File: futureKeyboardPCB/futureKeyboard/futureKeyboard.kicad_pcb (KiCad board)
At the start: 2 copper layers, 106 parts, among them J1 Conn_01x01, J10 Conn_01x02, J11 Conn_01x01, J12 Conn_01x01, J13 Conn_01x04, J14 Conn_01x06, J15 Conn_01x06, J16 Conn_01x01, J2 Conn_01x04, J3 Conn_01x01, J4 Conn_01x01, J5 Conn_01x04, J6 Conn_01x06, J7 Conn_01x06, J8 Conn_01x01, J9 Conn_01x01, P1 CONN_01X02, P2 CONN_01X06, P3 CONN_01X02, P4 CONN_01X06, Q1 2SC1815, Q2 2SC1815, Q3 2SC1815, Q4 2SC1815, Q5 2SC1815, Q6 2SC1815, SW1 SW_SPDT, SW10 SW_Push, SW11 SW_Push, SW12 SW_Push, SW13 SW_Push, SW14 SW_Push, SW15 SW_Push, SW16 SW_Push, SW17 SW_Push, SW18 SW_Push, SW19 SW_Push, SW2 SW_Push, SW20 SW_Push, SW21 SW_Push, SW22 SW_Push, SW23 SW_Push, SW24 SW_Push, SW25 SW_Push, SW3 SW_Push, SW4 SW_Push, SW5 SW_Push, SW6 SW_Push, SW7 SW_Push, SW8 SW_Push, SW9 SW_SPDT, U1 AMS1117-1.5, U2 ESP32, U3 AMS1117-1.5, U4 ESP32

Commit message: divide layors, make footprints, aligned footprints
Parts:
- removed RV1, RV2: R_POT, akizukit:S_POT_SMD
- added D11: LED, akizukit:2012LED, F.Cu at (17.9, 149.3)
- added GND22: WS2812B, akizukit:WS2812B, F.Cu at (184.2, 38.1)
- added J17: Conn_01x13, Connector_PinHeader_2.54mm:PinHeader_1x13_P2.54mm_Vertical_SMD_Pin1Left, F.Cu at (181.6, 116.8)
- added J18: Conn_01x13, Connector_PinHeader_2.54mm:PinHeader_1x13_P2.54mm_Vertical_SMD_Pin1Left, B.Cu at (288.3, 50.8)
- added J19: Conn_01x15, Connector_PinHeader_2.54mm:PinHeader_1x15_P2.54mm_Vertical_SMD_Pin1Left, F.Cu at (76.2, 154.9)
- added J20: Conn_01x15, Connector_PinHeader_2.54mm:PinHeader_1x15_P2.54mm_Vertical_SMD_Pin1Left, B.Cu at (124.5, 63.5)
- added J21: Conn_01x04, Connector_PinHeader_2.54mm:PinHeader_1x04_P2.54mm_Vertical_SMD_Pin1Left, F.Cu at (182.9, 144.8)
- added J22: Conn_01x04, Connector_PinHeader_2.54mm:PinHeader_1x04_P2.54mm_Vertical_SMD_Pin1Left, B.Cu at (163.8, 40.6)
- added J23: Conn_01x04, Connector_PinHeader_2.54mm:PinHeader_1x04_P2.54mm_Vertical_SMD_Pin1Left, F.Cu at (118.1, 157.5)
- added J24: Conn_01x04, Connector_PinHeader_2.54mm:PinHeader_1x04_P2.54mm_Vertical_SMD_Pin1Left, B.Cu at (24.1, 87.6)
- added R26: 1k, akizukit:SMD-1608, F.Cu at (243.6, 96.9)
- added R27: 1k, akizukit:SMD-1608, F.Cu at (17.5, 151.5)
- added U5: joystick, akizukit:joyStick, F.Cu at (208.3, 38.1)
- D10, D3, D4, D5, D7, D8, D9: footprint LED_SMD:LED_WS2812B_PLCC4_5.0x5.0mm_P3.2mm -> akizukit:WS2812B
- D2: value WS2812B -> LED; footprint LED_SMD:LED_WS2812B_PLCC4_5.0x5.0mm_P3.2mm -> akizukit:2012LED
- moved SW9 164.4 mm to (21.6, 172.7)
- moved C10 163.4 mm to (38.1, 168.9)
- moved J10 161.9 mm to (53.3, 157.5)
- moved J12 157.1 mm to (57.1, 161.3)
- moved P3 146.8 mm to (19.8, 168.6)
- moved U3 146.8 mm to (20.3, 157.2)
- moved J13 146.6 mm to (40.6, 133.3)
- moved J14 146.1 mm to (36.8, 133.3)
- moved SW11 142.5 mm to (104.1, 171.4)
- moved J9 139.9 mm to (49.5, 160.8)
- moved SW10 137.3 mm to (102.9, 182.9)
- moved U4 136.7 mm to (86.4, 143.5)
- moved Q5 132.8 mm to (26.7, 160.0)
- moved R19 130.7 mm to (98.0, 165.1)
- moved R15 129.7 mm to (31.8, 163.8), turned to 180 degrees
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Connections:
- C1 pad 2: GND -> /Sheet5F548957/GND2
- C10 pad 2: GND -> /Sheet5F548F88/GND
- C11 pad 2: GND -> /Sheet5F548F88/GND
- C12 pad 1: GND -> /Sheet5F548F88/GND
- C2 pad 2: GND -> /Sheet5F548957/GND2
- C3 pad 2: GND -> /Sheet5F548957/GND2
- C4 pad 2: GND -> /Sheet5F548957/GND2
- C5 pad 2: GND -> /Sheet5F548957/GND2
- C6 pad 1: GND -> /Sheet5F548957/GND2
- C7 pad 2: GND -> /Sheet5F548F88/GND
- C8 pad 2: GND -> /Sheet5F548F88/GND
- C9 pad 2: GND -> /Sheet5F548F88/GND
- D10 pad 1: /Sheet5F548F88/3v3 -> /Sheet5F548F88/3v32
- D10 pad 3: GND -> /Sheet5F548F88/GND2
- D2 pad 1: /Sheet5F548957/3v3 -> /Sheet5F548957/GND2
- D3 pad 1: /Sheet5F548957/3v3 -> /Sheet5F548957/3v32
- D3 pad 3: GND -> /Sheet5F548957/GND22
- D3 pad 4: Net-(D2-Pad2) -> Net-(D3-Pad4)
- D4 pad 1: /Sheet5F548957/3v3 -> /Sheet5F548957/3v32
- D4 pad 3: GND -> /Sheet5F548957/GND22
- D5 pad 1: /Sheet5F548957/3v3 -> /Sheet5F548957/3v32
- D5 pad 3: GND -> /Sheet5F548957/GND22
- D7 pad 1: /Sheet5F548F88/3v3 -> /Sheet5F548F88/3v32
- D7 pad 3: GND -> /Sheet5F548F88/GND2
- D7 pad 4: /Sheet5F548F88/LEDs -> /Sheet5F548F88/LEDs2
- D8 pad 1: /Sheet5F548F88/3v3 -> /Sheet5F548F88/3v32
- D8 pad 3: GND -> /Sheet5F548F88/GND2
- D9 pad 1: /Sheet5F548F88/3v3 -> /Sheet5F548F88/3v32
- D9 pad 3: GND -> /Sheet5F548F88/GND2
- J13 pad 2: GND -> /Sheet5F548F88/GND
- J14 pad 3: GND -> /Sheet5F548F88/GND
- J15 pad 3: GND -> /Sheet5F548F88/GND
- J16 pad 1: GND -> /Sheet5F548F88/GND
- J5 pad 2: GND -> /Sheet5F548957/GND2
- J6 pad 3: GND -> /Sheet5F548957/GND2
- J7 pad 3: GND -> /Sheet5F548957/GND2
- J8 pad 1: GND -> /Sheet5F548957/GND2
- P1 pad 1: GND -> /Sheet5F548957/GND2
- P2 pad 6: GND -> /Sheet5F548957/GND2
- P3 pad 1: GND -> /Sheet5F548F88/GND
- P4 pad 6: GND -> /Sheet5F548F88/GND
- Q3 pad 1: GND -> /Sheet5F548957/GND22
- Q3 pad 3: /Sheet5F548957/spk -> /Sheet5F548957/spk2
- Q6 pad 1: GND -> /Sheet5F548F88/GND2
- Q6 pad 3: /Sheet5F548F88/spk -> /Sheet5F548F88/spk2
- R10 pad 1: /Sheet5F548957/button1 -> /Sheet5F548957/button12
- R10 pad 2: /Sheet5F548957/3v3 -> /Sheet5F548957/3v32
- R11 pad 1: /Sheet5F548957/button2 -> /Sheet5F548957/button22
- R11 pad 2: /Sheet5F548957/3v3 -> /Sheet5F548957/3v32
- R12 pad 1: /Sheet5F548957/jx -> /Sheet5F548957/GND22
- R13 pad 1: /Sheet5F548957/jy -> Net-(R13-Pad1)
- R13 pad 2: Net-(R13-Pad2) -> /Sheet5F548957/GND22
- R18 pad 2: /Sheet5F548F88/3v3 -> /Sheet5F548F88/3v32
- R19 pad 2: GND -> /Sheet5F548F88/GND
- R20 pad 1: /Sheet5F548F88/r1 -> /Sheet5F548F88/r21
- R20 pad 2: GND -> /Sheet5F548F88/GND2
- R21 pad 1: /Sheet5F548F88/r2 -> /Sheet5F548F88/r22
- R21 pad 2: GND -> /Sheet5F548F88/GND2
- R22 pad 1: /Sheet5F548F88/r3 -> /Sheet5F548F88/r23
- R22 pad 2: GND -> /Sheet5F548F88/GND2
- R23 pad 1: /Sheet5F548F88/r4 -> /Sheet5F548F88/r24
- R23 pad 2: GND -> /Sheet5F548F88/GND2
- R24 pad 1: GND -> /Sheet5F548F88/GND2
- R24 pad 2: /Sheet5F548F88/button1 -> /Sheet5F548F88/button21
- R25 pad 1: GND -> /Sheet5F548F88/GND2
- R25 pad 2: /Sheet5F548F88/button2 -> /Sheet5F548F88/button22
- R5 pad 2: /Sheet5F548957/3v3 -> /Sheet5F548957/3v32
- R6 pad 2: GND -> /Sheet5F548957/GND2
- R7 pad 1: /Sheet5F548957/enter -> /Sheet5F548957/enter2
- R7 pad 2: /Sheet5F548957/3v3 -> /Sheet5F548957/3v32
- R8 pad 1: /Sheet5F548957/conv -> /Sheet5F548957/conv2
- R8 pad 2: /Sheet5F548957/3v3 -> /Sheet5F548957/3v32
- R9 pad 1: /Sheet5F548957/back -> /Sheet5F548957/back2
- R9 pad 2: /Sheet5F548957/3v3 -> /Sheet5F548957/3v32
- SW10 pad 1: GND -> /Sheet5F548F88/GND
- SW11 pad 1: GND -> /Sheet5F548F88/GND
- SW12 pad 1: /Sheet5F548F88/c1 -> /Sheet5F548F88/c12
- SW12 pad 2: /Sheet5F548F88/r1 -> /Sheet5F548F88/r21
- SW13 pad 1: /Sheet5F548F88/c1 -> /Sheet5F548F88/c12
- SW13 pad 2: /Sheet5F548F88/r2 -> /Sheet5F548F88/r22
- SW14 pad 1: /Sheet5F548F88/c1 -> /Sheet5F548F88/c12
- SW14 pad 2: /Sheet5F548F88/r3 -> /Sheet5F548F88/r23
- SW15 pad 1: /Sheet5F548F88/c1 -> /Sheet5F548F88/c12
- SW15 pad 2: /Sheet5F548F88/r4 -> /Sheet5F548F88/r24
- SW16 pad 1: /Sheet5F548F88/c2 -> /Sheet5F548F88/c22
- SW16 pad 2: /Sheet5F548F88/r1 -> /Sheet5F548F88/r21
- SW17 pad 1: /Sheet5F548F88/c2 -> /Sheet5F548F88/c22
- SW17 pad 2: /Sheet5F548F88/r2 -> /Sheet5F548F88/r22
- SW18 pad 1: /Sheet5F548F88/c2 -> /Sheet5F548F88/c22
- SW18 pad 2: /Sheet5F548F88/r3 -> /Sheet5F548F88/r23
- SW19 pad 1: /Sheet5F548F88/c2 -> /Sheet5F548F88/c22
- SW19 pad 2: /Sheet5F548F88/r4 -> /Sheet5F548F88/r24
- SW2 pad 1: GND -> /Sheet5F548957/GND2
- SW20 pad 1: /Sheet5F548F88/c3 -> /Sheet5F548F88/c23
- SW20 pad 2: /Sheet5F548F88/r1 -> /Sheet5F548F88/r21
- SW21 pad 1: /Sheet5F548F88/c3 -> /Sheet5F548F88/c23
- SW21 pad 2: /Sheet5F548F88/r2 -> /Sheet5F548F88/r22
- SW22 pad 1: /Sheet5F548F88/c3 -> /Sheet5F548F88/c23
- SW22 pad 2: /Sheet5F548F88/r3 -> /Sheet5F548F88/r23
- SW23 pad 1: /Sheet5F548F88/c3 -> /Sheet5F548F88/c23
- SW23 pad 2: /Sheet5F548F88/r4 -> /Sheet5F548F88/r24
- SW24 pad 1: /Sheet5F548F88/3v3 -> /Sheet5F548F88/3v32
- SW24 pad 2: /Sheet5F548F88/button1 -> /Sheet5F548F88/button21
- SW25 pad 1: /Sheet5F548F88/3v3 -> /Sheet5F548F88/3v32
- SW25 pad 2: /Sheet5F548F88/button2 -> /Sheet5F548F88/button22
- SW3 pad 1: GND -> /Sheet5F548957/GND2
- SW4 pad 1: /Sheet5F548957/enter -> /Sheet5F548957/enter2
- SW4 pad 2: GND -> /Sheet5F548957/GND22
- SW5 pad 1: /Sheet5F548957/conv -> /Sheet5F548957/conv2
- SW5 pad 2: GND -> /Sheet5F548957/GND22
- SW6 pad 1: /Sheet5F548957/back -> /Sheet5F548957/back2
- SW6 pad 2: GND -> /Sheet5F548957/GND22
- SW7 pad 1: /Sheet5F548957/button1 -> /Sheet5F548957/button12
- SW7 pad 2: GND -> /Sheet5F548957/GND22
- SW8 pad 1: /Sheet5F548957/button2 -> /Sheet5F548957/button22
- SW8 pad 2: GND -> /Sheet5F548957/GND22
- U1 pad 1: GND -> /Sheet5F548957/GND2
- U2 pad 1: GND -> /Sheet5F548957/GND2
- U2 pad 15: GND -> /Sheet5F548957/GND2
- U2 pad 38: GND -> /Sheet5F548957/GND2
- U3 pad 1: GND -> /Sheet5F548F88/GND
- U4 pad 1: GND -> /Sheet5F548F88/GND
- U4 pad 15: GND -> /Sheet5F548F88/GND
- U4 pad 38: GND -> /Sheet5F548F88/GND

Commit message: fix circuit bags, and placement electric parts
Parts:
- added J25: Conn_01x02, Connector_PinHeader_2.54mm:PinHeader_1x02_P2.54mm_Vertical, F.Cu at (158.8, 26.7)
- J17, J18: value Conn_01x13 -> Conn_01x15; footprint Connector_PinHeader_2.54mm:PinHeader_1x13_P2.54mm_Vertical_SMD_Pin1Left -> Connector_PinHeader_2.54mm:PinHeader_1x15_P2.54mm_Vertical_SMD_Pin1Left
- J2: value Conn_01x04 -> Conn_01x02; footprint Connector_PinHeader_2.54mm:PinHeader_1x04_P2.54mm_Vertical -> Connector_PinHeader_2.54mm:PinHeader_1x02_P2.54mm_Vertical
- moved C1 120.0 mm to (141.6, 176.5)
- moved C6 120.0 mm to (147.5, 178.5)
- moved D2 120.0 mm to (155.7, 175.9)
- moved U1 120.0 mm to (153.0, 188.0)
- moved C4 120.0 mm to (136.5, 181.6)
- moved R26 120.0 mm to (155.3, 178.2)
- moved C5 120.0 mm to (143.2, 178.5)
- moved P1 120.0 mm to (148.0, 188.1)
- moved SW1 120.0 mm to (164.5, 180.3)
- moved J18 119.7 mm to (168.9, 41.9)
- moved P2 96.0 mm to (238.8, 179.1), turned to 180 degrees
- moved J8 91.5 mm to (146.1, 132.7)
- moved J17 88.5 mm to (188.0, 205.1), turned to 270 degrees
- moved J1 87.9 mm to (146.1, 130.2)
- moved J3 87.7 mm to (149.9, 130.2)
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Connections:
- J17 pad 12: /Sheet5F548957/GND2 -> /Sheet5F548957/dummy1
- J17 pad 13: /Sheet5F548957/3v3 -> /Sheet5F548957/dummy2
- J18 pad 12: /Sheet5F548957/GND22 -> /Sheet5F548957/dummy12
- J18 pad 13: /Sheet5F548957/3v32 -> /Sheet5F548957/dummy22
- U2 pad 11: Net-(J2-Pad1) -> /Sheet5F548957/dummy1
- U2 pad 12: Net-(J2-Pad2) -> /Sheet5F548957/dummy2
- U2 pad 13: Net-(J2-Pad3) -> Net-(J2-Pad2)
- U2 pad 14: Net-(J2-Pad4) -> Net-(J2-Pad1)

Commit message: complete placement electronic parts
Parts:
- added h**: HOLE_2.1mm, akizukit:HOLE_3.2mm_nopad, F.Cu at (203.3, 154.9)
- added h**: HOLE_2.1mm, akizukit:HOLE_3.2mm_nopad, F.Cu at (203.3, 119.9)
- added h**: HOLE_2.1mm, akizukit:HOLE_3.2mm_nopad, F.Cu at (248.3, 154.9)
- added h**: HOLE_2.1mm, akizukit:HOLE_3.2mm_nopad, F.Cu at (248.3, 119.9)
- added h**: HOLE_2.1mm, akizukit:HOLE_3.2mm_nopad, F.Cu at (61.0, 154.9)
- added h**: HOLE_2.1mm, akizukit:HOLE_3.2mm_nopad, F.Cu at (61.0, 119.9)
- added h**: HOLE_2.1mm, akizukit:HOLE_3.2mm_nopad, F.Cu at (106.0, 119.9)
- added h**: HOLE_2.1mm, akizukit:HOLE_3.2mm_nopad, F.Cu at (106.0, 154.9)
- C1, C7, D1, D6, J25, LS1, LS2, Q3, Q6, R1, R10, R11, R12, R13, R14, R15, R18, R2, R20, R21, R22, R23, R24, R25, R5, R7, R8, R9, SW10, SW11, SW2, SW3, U2, U3, U4: moved to B.Cu
- P2, P4: footprint Connector_PinHeader_2.54mm:PinHeader_1x06_P2.54mm_Vertical -> Connector_PinHeader_2.54mm:PinHeader_1x06_P2.54mm_Horizontal
- U1: footprint akizukit:AZ1086H -> Package_TO_SOT_SMD:SOT-223-3_TabPin2; moved to B.Cu
- moved C1 111.8 mm to (247.7, 141.0)
- moved R20 107.6 mm to (109.9, 34.3), turned to 90 degrees
- moved P1 106.0 mm to (242.6, 140.3), turned to 180 degrees
- moved U1 97.1 mm to (240.7, 146.1), turned to 180 degrees
- moved C5 95.4 mm to (222.2, 125.1), turned to 270 degrees
- moved C6 93.5 mm to (224.2, 125.1), turned to 90 degrees
- moved SW1 91.9 mm to (248.9, 144.1)
- moved D2 90.6 mm to (225.4, 118.1), turned to 180 degrees
- moved J25 90.1 mm to (242.6, 59.7), turned to 180 degrees
- moved C4 89.8 mm to (205.7, 124.4), turned to 270 degrees
- moved R21 87.0 mm to (109.9, 54.6), turned to 90 degrees
- moved J2 85.9 mm to (226.7, 146.1)
- moved R22 84.1 mm to (109.9, 74.9), turned to 90 degrees
- moved J17 82.4 mm to (233.7, 136.5), turned to 0 degrees
- moved P3 81.3 mm to (100.3, 140.3), turned to 180 degrees
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- renumbered GND22 to D2
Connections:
- C1 pad 1: /Sheet5F548957/Vcc -> Net-(C1-Pad1)
- C7 pad 1: /Sheet5F548F88/Vcc -> Net-(C7-Pad1)
- J17 pad 10: /Sheet5F548957/button1 -> /Sheet5F548957/dummy1
- J17 pad 11: /Sheet5F548957/button2 -> /Sheet5F548957/dummy2
- J17 pad 12: /Sheet5F548957/dummy1 -> /Sheet5F548957/button1
- J17 pad 13: /Sheet5F548957/dummy2 -> /Sheet5F548957/button2
- J17 pad 7: /Sheet5F548957/back -> /Sheet5F548957/enter
- J17 pad 9: /Sheet5F548957/enter -> /Sheet5F548957/back
- J18 pad 10: /Sheet5F548957/button12 -> /Sheet5F548957/dummy12
- J18 pad 11: /Sheet5F548957/button22 -> /Sheet5F548957/dummy22
- J18 pad 12: /Sheet5F548957/dummy12 -> /Sheet5F548957/button12
- J18 pad 13: /Sheet5F548957/dummy22 -> /Sheet5F548957/button22
- Q2 pad 1: /Sheet5F548957/IO0 -> /Sheet5F548957/DTR
- Q2 pad 2: /Sheet5F548957/DTR -> /Sheet5F548957/IO0
- Q5 pad 1: /Sheet5F548F88/IO0 -> /Sheet5F548F88/DTR
- Q5 pad 2: /Sheet5F548F88/DTR -> /Sheet5F548F88/IO0
- SW1 pad 3: /Sheet5F548957/Vcc -> Net-(C1-Pad1)
- SW9 pad 3: /Sheet5F548F88/Vcc -> Net-(C7-Pad1)
- U1 pad 3: /Sheet5F548957/Vcc -> Net-(C1-Pad1)
- U3 pad 3: /Sheet5F548F88/Vcc -> Net-(C7-Pad1)

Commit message: complete footprint placement
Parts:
- moved LS1 209.8 mm to (26.0, 114.3)
- moved R10 209.8 mm to (42.5, 93.3)
- moved R12 209.8 mm to (43.8, 105.4)
- moved R13 209.8 mm to (41.9, 105.4)
- moved R7 209.8 mm to (22.2, 121.3)
- moved R8 209.8 mm to (43.8, 123.8)
- moved SW4 209.8 mm to (26.0, 121.3)
- moved SW7 209.8 mm to (41.9, 92.7)
- moved SW8 209.8 mm to (50.8, 92.7)
- moved D1 209.8 mm to (19.7, 110.5)
- moved J25 209.8 mm to (41.3, 118.7)
- moved Q3 209.8 mm to (14.0, 115.6)
- moved R11 209.8 mm to (45.1, 93.3)
- moved R5 209.8 mm to (14.0, 118.1)
- moved R9 209.8 mm to (19.7, 99.7)
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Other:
- board outline added: 168.9 x 88.3 mm

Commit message: complete PCB
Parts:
- removed h** (x8): HOLE_2.1mm, akizukit:HOLE_3.2mm_nopad
- added J26: Conn_01x01, akizukit:HOLE_3.2mm_nopad, F.Cu at (116.8, 75.5)
- added J27: Conn_01x01, akizukit:HOLE_3.2mm_nopad, F.Cu at (71.8, 29.8)
- added J28: Conn_01x01, akizukit:HOLE_3.2mm_nopad, F.Cu at (71.8, 75.5)
- added J29: Conn_01x01, akizukit:HOLE_3.2mm_nopad, F.Cu at (116.8, 29.8)
- added J30: Conn_01x01, akizukit:HOLE_3.2mm_nopad, F.Cu at (71.8, 110.5)
- added J31: Conn_01x01, akizukit:HOLE_3.2mm_nopad, F.Cu at (71.8, 64.8)
- added J32: Conn_01x01, akizukit:HOLE_3.2mm_nopad, F.Cu at (116.8, 110.5)
- added J33: Conn_01x01, akizukit:HOLE_3.2mm_nopad, F.Cu at (116.8, 64.8)
- moved J10 45.7 mm to (96.5, 101.6)
- moved J11 45.7 mm to (75.6, 101.6)
- moved J12 45.7 mm to (73.0, 101.6)
- moved J14 45.7 mm to (91.4, 101.6)
- moved SW9 45.7 mm to (117.5, 99.7)
- moved J17 45.7 mm to (102.2, 46.4)
- moved J20 45.7 mm to (171.4, 46.4)
- moved J21 45.7 mm to (73.0, 46.4)
- moved J24 45.7 mm to (142.2, 46.4)
- moved U5 45.7 mm to (55.2, 62.2)
- moved C1 45.7 mm to (116.2, 50.8)
- moved C11 45.7 mm to (86.4, 81.3)
- moved C12 45.7 mm to (86.4, 83.2)
- moved C5 45.7 mm to (90.8, 34.9)
- moved C6 45.7 mm to (92.7, 34.9)
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- renumbered D2 to GND22
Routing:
- net /Sheet5F548F88/GND2: track 0.00 -> 258.6 mm, vias 0 -> 1
- net /Sheet5F548F88/GND: track 0.00 -> 213.9 mm, vias 0 -> 1
- net /Sheet5F548F88/3v3: track 0.00 -> 212.5 mm
- net /Sheet5F548F88/3v32: track 0.00 -> 205.8 mm, vias 0 -> 2
- net /Sheet5F548957/3v32: track 0.00 -> 195.7 mm
- net /Sheet5F548957/GND2: track 0.00 -> 192.4 mm, vias 0 -> 3
- net /Sheet5F548957/GND22: track 0.00 -> 165.6 mm, vias 0 -> 1
- net /Sheet5F548957/3v3: track 0.00 -> 150.5 mm, vias 0 -> 2
- net /Sheet5F548F88/c12: track 0.00 -> 119.6 mm
- net /Sheet5F548F88/r24: track 0.00 -> 89.7 mm
- net /Sheet5F548F88/r23: track 0.00 -> 86.4 mm
- net /Sheet5F548957/EN: track 0.00 -> 84.6 mm, vias 0 -> 1
- net /Sheet5F548F88/r21: track 0.00 -> 79.0 mm
- net /Sheet5F548F88/c22: track 0.00 -> 75.0 mm
- net /Sheet5F548F88/IO0: track 0.00 -> 73.2 mm
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- added copper zone on B.Cu, net /Sheet5F548957/GND2
- added copper zone on F.Cu, net /Sheet5F548957/GND2
- added copper zone on B.Cu, net /Sheet5F548957/GND22
- added copper zone on F.Cu, net /Sheet5F548957/GND22
- added copper zone on B.Cu, net /Sheet5F548F88/GND
- added copper zone on F.Cu, net /Sheet5F548F88/GND
- added copper zone on B.Cu, net /Sheet5F548F88/GND2
- added copper zone on F.Cu, net /Sheet5F548F88/GND2
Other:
- outline, holes or cut-outs redrawn
- net class Power added: clearance 0.25, trace_width 0.35, via_dia 0.8, via_drill 0.4

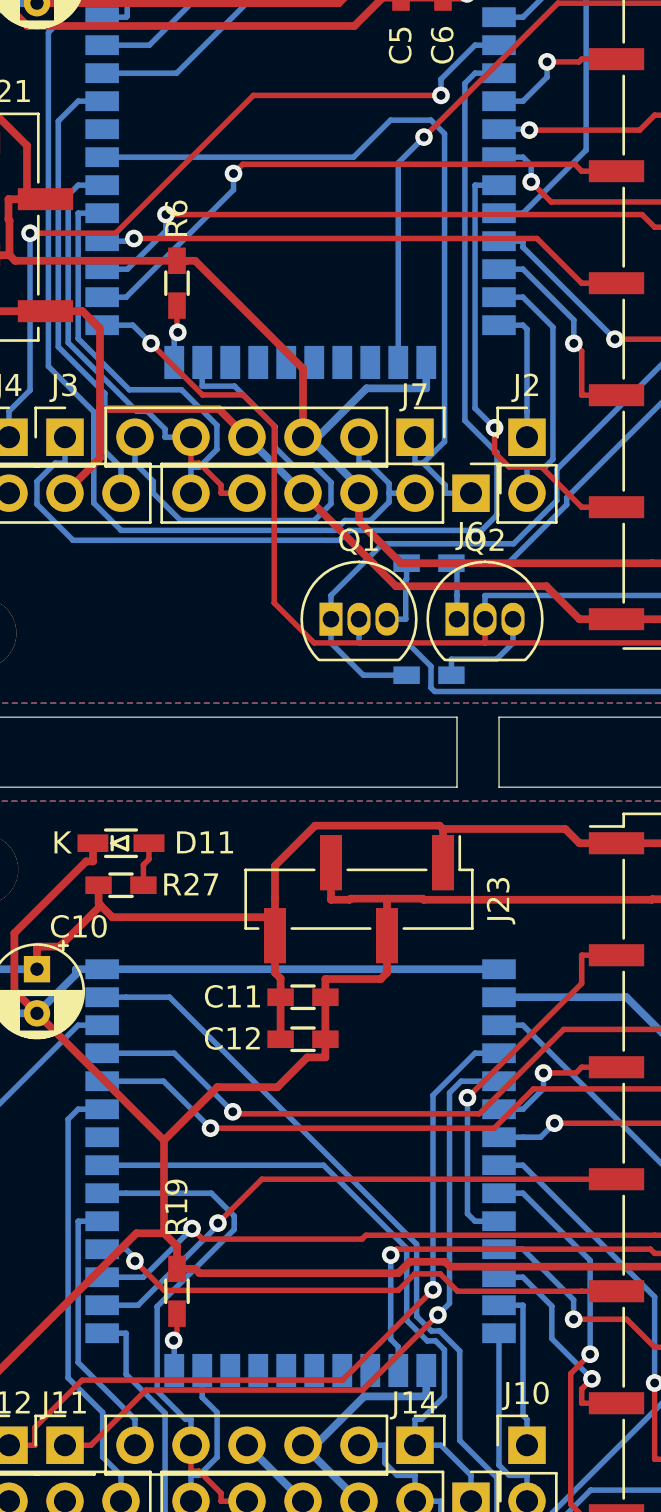
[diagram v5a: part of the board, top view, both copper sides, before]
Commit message: add Logo
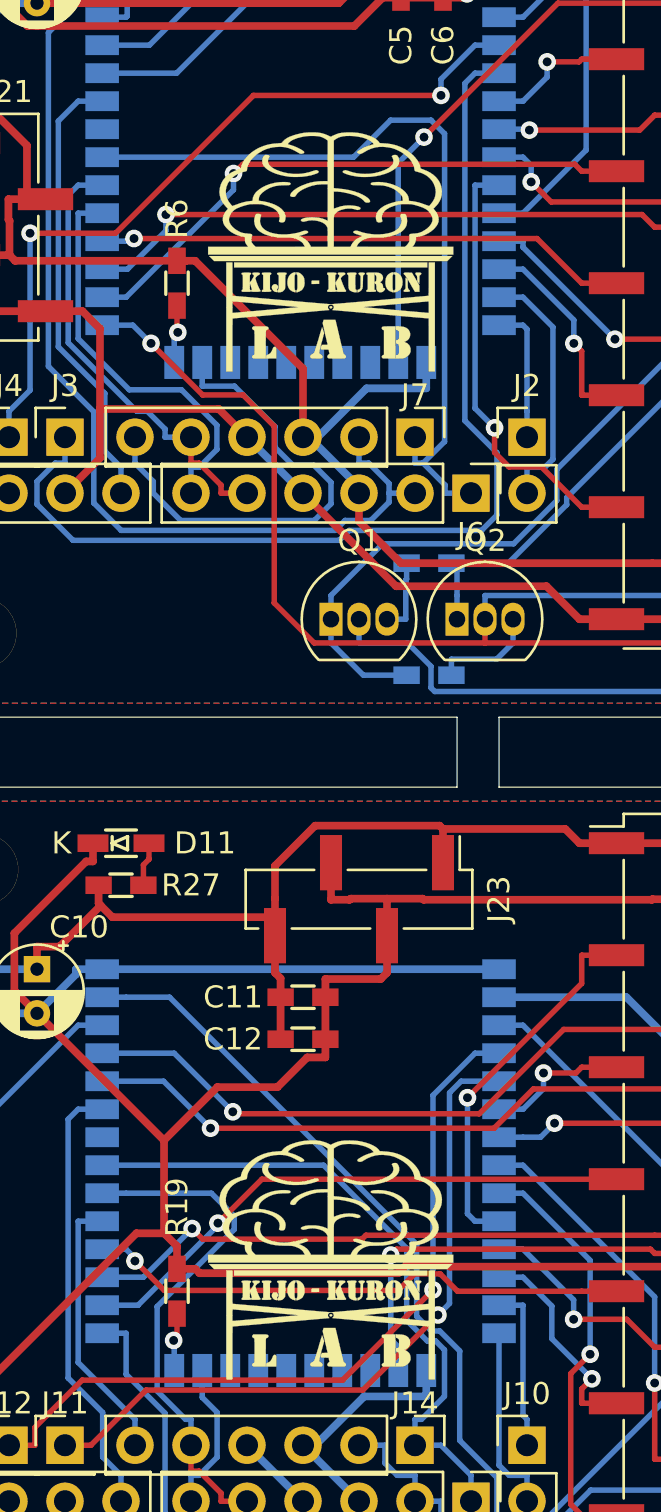
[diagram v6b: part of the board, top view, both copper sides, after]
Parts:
- added G***: LOGO, Symbol:Kijo-Kuron-LAB_small2, B.Cu at (151.1, 102.2)
- added G***: LOGO, Symbol:Kijo-Kuron-LAB_small, B.Cu at (59.1, 93.3)
- added G***: LOGO, Symbol:Kijo-Kuron-LAB_small, F.Cu at (87.6, 48.3)
- added G***: LOGO, Symbol:Kijo-Kuron-LAB_small, F.Cu at (87.6, 94.0)
